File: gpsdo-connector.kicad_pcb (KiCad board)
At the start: 2 copper layers, 100 x 133.5 mm, 41 parts, among them J101 NEB21R, J102 Conn_02x05_Odd_Even, J103 Conn_02x05_Top_Bottom, J104 FPC-50-0.5MM, J105 Conn_02x03_Top_Bottom, J106 Conn_02x03_Top_Bottom, J107 Conn_02x05_Top_Bottom, J108 Conn_01x02, J109 Conn_02x05_Top_Bottom, U201 APE8865N-33-HF-3, U202 LMR14030SDDAR, U301 MAX3232

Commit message: VE7XEN BBB Carrier rev 1
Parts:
- removed C201, C210: 4.7u, Capacitor_SMD:C_0805_2012Metric
- removed C202: 270pF, Capacitor_SMD:C_0805_2012Metric
- removed C203: 100nF, Capacitor_SMD:C_0805_2012Metric
- removed C204, C205: 6.8u, Capacitor_SMD:C_1206_3216Metric
- removed C206, C207: 39u, Capacitor_SMD:CP_Elec_5x5.9
- removed C208: 200n, Capacitor_SMD:C_0805_2012Metric
- removed C209: 10nF, Capacitor_SMD:C_0805_2012Metric
- removed C211: 47u, Capacitor_SMD:CP_Elec_5x5.9
- removed C301, C302, C303, C304, C305: 100n, Capacitor_SMD:C_0805_2012Metric
- removed D201: B330BE-13, Diode_SMD:D_SMB
- removed D202: ES2BA-13-F, Diode_SMD:D_SMA
- removed H101: MountingHole, MountingHole:MountingHole_3.2mm_M3_DIN965
- removed J101: NEB21R, project:NEB21R
- removed J102: Conn_02x05_Odd_Even, Connector_IDC:IDC-Header_2x05_P2.54mm_Vertical
- removed J103, J107: Conn_02x05_Top_Bottom, Connector_IDC:IDC-Header_2x05_P2.54mm_Vertical
- removed J105, J106: Conn_02x03_Top_Bottom, Connector_PinHeader_2.54mm:PinHeader_2x03_P2.54mm_Vertical
- removed J108: Conn_01x02, Connector_PinHeader_2.54mm:PinHeader_1x02_P2.54mm_Vertical
- removed J109: Conn_02x05_Top_Bottom, Connector_PinHeader_2.54mm:PinHeader_2x05_P2.54mm_Vertical
- removed L201: 2.2µH, Inductor_SMD:L_Coilcraft_XAL5030
- removed L202: 1u, Inductor_SMD:L_1206_3216Metric
- removed NT201: Net-Tie_2, NetTie:NetTie-2_SMD_Pad2.0mm
- removed R201: 25k5, Resistor_SMD:R_0805_2012Metric
- removed R202: 14k, Resistor_SMD:R_0805_2012Metric_Pad1.15x1.40mm_HandSolder
- removed R203: 10k, Resistor_SMD:R_0805_2012Metric_Pad1.15x1.40mm_HandSolder
- removed RV201: 50k, project:Trimpot_Bourns_3313J-1
- removed U201: APE8865N-33-HF-3, Package_TO_SOT_SMD:SOT-23
- removed U202: LMR14030SDDAR, Package_SO:TI_SO-PowerPAD-8
- removed U301: MAX3232, Package_SO:SOIC-16_3.9x9.9mm_P1.27mm
- added BT1: CR2032, project:CR2032-BS-6-1, B.Cu at (83.3, 92.2)
- added C1: 100nF, Capacitor_SMD:C_0805_2012Metric_Pad1.18x1.45mm_HandSolder, F.Cu at (56.6, 156.5)
- added C10: 47uF, Capacitor_SMD:C_1206_3216Metric_Pad1.33x1.80mm_HandSolder, F.Cu at (71.3, 127.8)
- added C11: 47uF, Capacitor_SMD:C_1206_3216Metric_Pad1.33x1.80mm_HandSolder, F.Cu at (71.3, 125.2)
- added C12: 100nF, Capacitor_SMD:C_0805_2012Metric_Pad1.18x1.45mm_HandSolder, F.Cu at (71.3, 122.8)
- added C13: 100n, Capacitor_SMD:C_0805_2012Metric_Pad1.18x1.45mm_HandSolder, F.Cu at (80.3, 93.2)
- added C14: 100n, Capacitor_SMD:C_0805_2012Metric_Pad1.18x1.45mm_HandSolder, F.Cu at (80.3, 82.5)
- added C15: 100n, Capacitor_SMD:C_0805_2012Metric_Pad1.18x1.45mm_HandSolder, F.Cu at (84.3, 93.2)
- added C16: 100n, Capacitor_SMD:C_0805_2012Metric_Pad1.18x1.45mm_HandSolder, F.Cu at (77.6, 89.5)
- added C17: 100n, Capacitor_SMD:C_0805_2012Metric_Pad1.18x1.45mm_HandSolder, F.Cu at (88.3, 93.2)
- added C18: 10n, Capacitor_SMD:C_0805_2012Metric_Pad1.18x1.45mm_HandSolder, F.Cu at (99.3, 139.0)
- added C19: 1uF, Capacitor_SMD:C_1206_3216Metric_Pad1.33x1.80mm_HandSolder, F.Cu at (90.8, 129.2)
- added C2: 100nF, Capacitor_SMD:C_0805_2012Metric_Pad1.18x1.45mm_HandSolder, F.Cu at (90.3, 79.0)
- added C20: 47p, Capacitor_SMD:C_0805_2012Metric_Pad1.18x1.45mm_HandSolder, F.Cu at (95.1, 140.5)
- added C21: 10pF, Capacitor_SMD:C_0805_2012Metric_Pad1.18x1.45mm_HandSolder, F.Cu at (97.8, 103.0)
- added C22: 100nF, Capacitor_SMD:C_0805_2012Metric_Pad1.18x1.45mm_HandSolder, F.Cu at (97.3, 109.2)
- added C23: 100nF, Capacitor_SMD:C_0805_2012Metric_Pad1.18x1.45mm_HandSolder, F.Cu at (92.6, 121.8)
- added C24: 100nF, Capacitor_SMD:C_0805_2012Metric_Pad1.18x1.45mm_HandSolder, F.Cu at (96.1, 115.5)
- added C3: 10uF, Capacitor_SMD:C_1206_3216Metric_Pad1.33x1.80mm_HandSolder, F.Cu at (62.0, 133.4)
- added C4: 10uF, Capacitor_SMD:C_1206_3216Metric_Pad1.33x1.80mm_HandSolder, F.Cu at (59.5, 133.4)
- added C5: 10uF, Capacitor_SMD:C_1206_3216Metric_Pad1.33x1.80mm_HandSolder, F.Cu at (62.0, 138.7)
- added C6: 10uF, Capacitor_SMD:C_1206_3216Metric_Pad1.33x1.80mm_HandSolder, F.Cu at (59.5, 138.7)
- added C7: 10nF, Capacitor_SMD:C_0805_2012Metric_Pad1.18x1.45mm_HandSolder, F.Cu at (74.3, 136.0)
- added C8: 100nF, Capacitor_SMD:C_0805_2012Metric_Pad1.18x1.45mm_HandSolder, F.Cu at (64.6, 130.8)
- added C9: 330pF, Capacitor_SMD:C_0805_2012Metric_Pad1.18x1.45mm_HandSolder, F.Cu at (79.8, 134.8)
- added D1: LED, LED_SMD:LED_0805_2012Metric_Pad1.15x1.40mm_HandSolder, F.Cu at (53.1, 78.5)
- added D2: LED, LED_SMD:LED_0805_2012Metric_Pad1.15x1.40mm_HandSolder, F.Cu at (53.1, 73.2)
- added D3: LED, LED_SMD:LED_0805_2012Metric_Pad1.15x1.40mm_HandSolder, F.Cu at (53.1, 83.8)
- added D4: SS54, Diode_SMD:D_SMA, F.Cu at (68.3, 54.2)
- added D5: SS54, Diode_SMD:D_SMA, F.Cu at (70.3, 131.0)
- added D6: BAV70, Package_TO_SOT_SMD:SOT-23, F.Cu at (100.6, 110.2)
- added J1: DC-005A-2.5A-2.0, project:DC-005A-2.5A-2.0, F.Cu at (64.3, 44.0)
- added J2: SQ_OUT, project:DOSIN-801-0080, F.Cu at (105.8, 154.2)
- added J3: SINE_OUT, project:DOSIN-801-0080, F.Cu at (89.8, 154.2)
- added J4: GPS_ACT, Connector_PinHeader_2.54mm:PinHeader_1x02_P2.54mm_Vertical, F.Cu at (114.6, 53.5)
- added J5: MASTER, Connector_PinHeader_2.54mm:PinHeader_1x02_P2.54mm_Vertical, F.Cu at (54.4, 53.5)
- added L1: 1u, Inductor_SMD:L_1206_3216Metric_Pad1.22x1.90mm_HandSolder, F.Cu at (68.3, 61.2)
- added L2: 4.7uH, Inductor_SMD:L_Abracon_ASPI-0630LR, F.Cu at (78.3, 128.8)
- added L3: 10u, Inductor_SMD:L_1206_3216Metric_Pad1.22x1.90mm_HandSolder, F.Cu at (98.8, 141.5)
- added L4: 10u, Inductor_SMD:L_1206_3216Metric_Pad1.22x1.90mm_HandSolder, F.Cu at (91.3, 141.5)
- added MH2: MountingHole_3.2mm_M3_DIN965, MountingHole:MountingHole_3.2mm_M3_DIN965, F.Cu at (60.3, 52.4)
- added MH3: MountingHole_3.2mm_M3_DIN965, MountingHole:MountingHole_3.2mm_M3_DIN965, F.Cu at (105.4, 118.4)
- added MH4: MountingHole_3.2mm_M3_DIN965, MountingHole:MountingHole_3.2mm_M3_DIN965, F.Cu at (63.5, 118.4)
- added NT1: Net-Tie_2, NetTie:NetTie-2_SMD_Pad2.0mm, F.Cu at (81.8, 142.0)
- added NT2: Net-Tie_2, NetTie:NetTie-2_SMD_Pad2.0mm, F.Cu at (81.8, 139.8)
- added P8: BeagleBone_Black_Header, Connector_PinHeader_2.54mm:PinHeader_2x23_P2.54mm_Vertical, B.Cu at (61.6, 57.4)
- added P9: BeagleBone_Black_Header, Connector_PinHeader_2.54mm:PinHeader_2x23_P2.54mm_Vertical, B.Cu at (109.9, 57.4)
- added R1: 220, Resistor_SMD:R_0805_2012Metric_Pad1.20x1.40mm_HandSolder, F.Cu at (55.6, 78.5)
- added R10: 47, Resistor_SMD:R_0805_2012Metric_Pad1.20x1.40mm_HandSolder, F.Cu at (99.6, 135.5)
- added R11: 47, Resistor_SMD:R_0805_2012Metric_Pad1.20x1.40mm_HandSolder, F.Cu at (102.1, 135.5)
- added R12: 5.6k, Resistor_SMD:R_0805_2012Metric_Pad1.20x1.40mm_HandSolder, F.Cu at (115.6, 76.8)
- added R13: 5.6k, Resistor_SMD:R_0805_2012Metric_Pad1.20x1.40mm_HandSolder, F.Cu at (113.3, 76.8)
- added R14: 47, Resistor_SMD:R_0805_2012Metric_Pad1.20x1.40mm_HandSolder, F.Cu at (89.6, 116.0)
- added R15: 47, Resistor_SMD:R_0805_2012Metric_Pad1.20x1.40mm_HandSolder, F.Cu at (96.8, 121.0)
- added R16: 47, Resistor_SMD:R_0805_2012Metric_Pad1.20x1.40mm_HandSolder, F.Cu at (105.8, 140.5)
- added R2: 220, Resistor_SMD:R_0805_2012Metric_Pad1.20x1.40mm_HandSolder, F.Cu at (55.6, 73.2)
- added R3: 220, Resistor_SMD:R_0805_2012Metric_Pad1.20x1.40mm_HandSolder, F.Cu at (55.6, 83.8)
- added R4: 10k, Resistor_SMD:R_0805_2012Metric_Pad1.20x1.40mm_HandSolder, F.Cu at (68.3, 72.2)
- added R5: 15k, Resistor_SMD:R_0805_2012Metric_Pad1.20x1.40mm_HandSolder, F.Cu at (66.6, 140.2)
- added R6: 12k, Resistor_SMD:R_0805_2012Metric_Pad1.20x1.40mm_HandSolder, F.Cu at (76.6, 136.0)
- added R7: 75k, Resistor_SMD:R_0805_2012Metric_Pad1.20x1.40mm_HandSolder, F.Cu at (79.8, 137.0)
- added R8: 47, Resistor_SMD:R_0805_2012Metric_Pad1.20x1.40mm_HandSolder, F.Cu at (94.6, 135.5)
- added R9: 47, Resistor_SMD:R_0805_2012Metric_Pad1.20x1.40mm_HandSolder, F.Cu at (97.1, 135.5)
- added RV1: 20k, project:Trimpot_Bourns_3313J-1, F.Cu at (84.6, 135.8)
- added U1: LM75B, Package_SO:MSOP-8_3x3mm_P0.65mm, F.Cu at (53.6, 155.2)
- added U2: LMR14030SDDAR, Package_SO:TI_SO-PowerPAD-8, F.Cu at (68.5, 136.0)
- added U3: MAX3232, Package_SO:SOIC-16_3.9x9.9mm_P1.27mm, F.Cu at (84.3, 87.8)
- added U4: 74HC04, Package_SO:SOIC-14_3.9x8.7mm_P1.27mm, F.Cu at (97.1, 129.2)
- added U5: PCF8563T, Package_SO:SOIC-8_3.9x4.9mm_P1.27mm, F.Cu at (93.3, 107.8)
- added U6: MS5351M, Package_SO:MSOP-10_3x3mm_P0.5mm, F.Cu at (92.8, 117.2)
- added Y1: 32.768k, Crystal:Crystal_SMD_3215-2Pin_3.2x1.5mm, F.Cu at (94.6, 102.0)
- H2: renamed from H102; moved to B.Cu
- H3: renamed from H103; moved to B.Cu
- H4: renamed from H104; moved to B.Cu
- J6: renamed from J104; footprint Connector_FFC-FPC:Molex_54132-5033_1x50-1MP_P0.5mm_Horizontal -> Connector_FFC-FPC:Hirose_FH12-50S-0.5SH_1x50-1MP_P0.50mm_Horizontal
- moved H2 178.8 mm to (53.9, 65.4), turned to 180 degrees
- moved H4 178.8 mm to (53.9, 140.2), turned to 180 degrees
- moved J6 106.5 mm to (89.3, 69.1), turned to 180 degrees
- moved H3 91.0 mm to (110.5, 140.2), turned to 180 degrees
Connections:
- J6 pad 10: GND -> unconnected-(J6-Pad10)
- J6 pad 11: GND -> unconnected-(J6-Pad10)
- J6 pad 14: /UART_TX -> /GPIO[2]
- J6 pad 15: /UART_RX -> /GPIO[3]
- J6 pad 20: Net-(J104-Pad20) -> unconnected-(J6-Pad20)
- J6 pad 22: Net-(J104-Pad22) -> unconnected-(J6-Pad22)
- J6 pad 24: Net-(J104-Pad24) -> unconnected-(J6-Pad24)
- J6 pad 26: Net-(J104-Pad26) -> unconnected-(J6-Pad26)
- J6 pad 32: Net-(J104-Pad32) -> unconnected-(J6-Pad32)
- J6 pad 33: Net-(J104-Pad33) -> unconnected-(J6-Pad33)
- J6 pad 35: Net-(J104-Pad35) -> unconnected-(J6-Pad35)
- J6 pad 36: Net-(J104-Pad36) -> unconnected-(J6-Pad36)
- J6 pad 37: /OUTP_ACT -> /GPIO[60]
- J6 pad 38: Net-(J104-Pad38) -> unconnected-(J6-Pad38)
- J6 pad 39: /MACT -> /GPIO[40]
- J6 pad 41: /RESET -> /GPIO[51]
- J6 pad 45: Net-(J104-Pad45) -> unconnected-(J6-Pad45)
- J6 pad 47: Net-(J104-Pad47) -> unconnected-(J6-Pad47)
- J6 pad 49: /UART_TX_HS -> /GPIO[30]
- J6 pad 8: Net-(J104-Pad8) -> unconnected-(J6-Pad8)
- J6 pad 9: GND -> unconnected-(J6-Pad10)
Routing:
- net +3V3: track 15.4 -> 277.2 mm, vias 0 -> 8
- net /I2C2.SDA: track 0.00 -> 132.8 mm, vias 0 -> 2
- net /I2C2.SCL: track 0.00 -> 131.9 mm
- net GNDS: track 48.3 -> 138.2 mm, vias 25 -> 37
- net Net-(C5-Pad1): track 0.00 -> 85.4 mm, vias 0 -> 6
- net /GPIO[65]: track 0.00 -> 56.4 mm, vias 0 -> 2
- net Net-(J6-Pad43): track 0.00 -> 40.9 mm, vias 0 -> 2
- net /GPIO[30]: track 0.00 -> 37.2 mm, vias 0 -> 1
- net /Clock Generation/CLKIN: track 0.00 -> 36.3 mm
- net Net-(J106-Pad6): track 34.1 -> 0.00 mm, vias 2 -> 0
- net Net-(J106-Pad5): track 34.0 -> 0.00 mm, vias 2 -> 0
- net Net-(R16-Pad2): track 0.00 -> 33.4 mm
- net /Clock Generation/10M Filter/10M_IN: track 0.00 -> 31.7 mm
- net /GPIO[51]: track 0.00 -> 31.4 mm, vias 0 -> 1
- net +5V: track 103.5 -> 134.3 mm, vias 2 -> 3
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- added copper zone on F.Cu, net Net-(C5-Pad1)
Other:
- board size 100 x 133.5 mm -> 70 x 121.5 mm
- net class Default removed
- board text added: "1"
- board text added: "12-15V"
- board text added: "50"
- board text added: "Note: due to to way pin numbers work on the BBB, the connectors are actually 2.54mm pin headers with the 3D models overridden."
- board text added: "VE7XEN UCCM+BBB Carrier rev 1 2022-10-07"

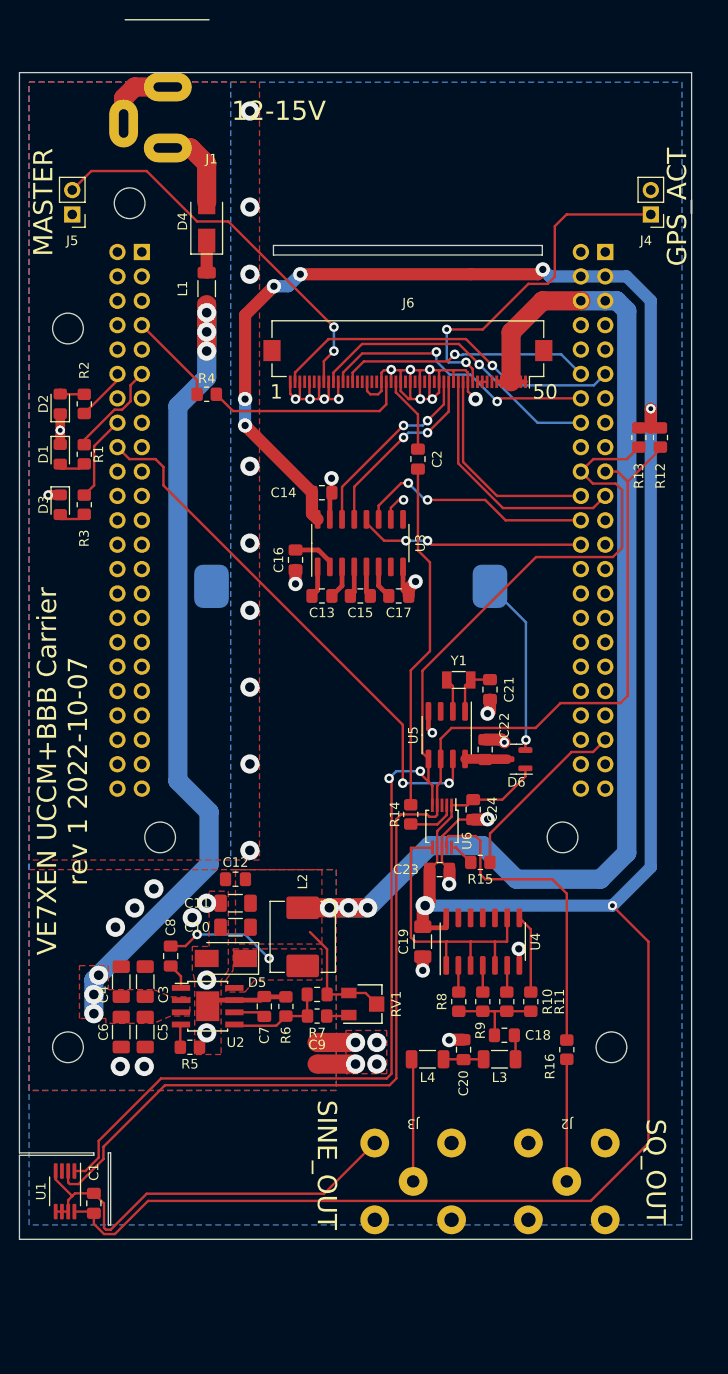
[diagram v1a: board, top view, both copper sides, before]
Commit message: rev 1 DFM fixes, kibot automation
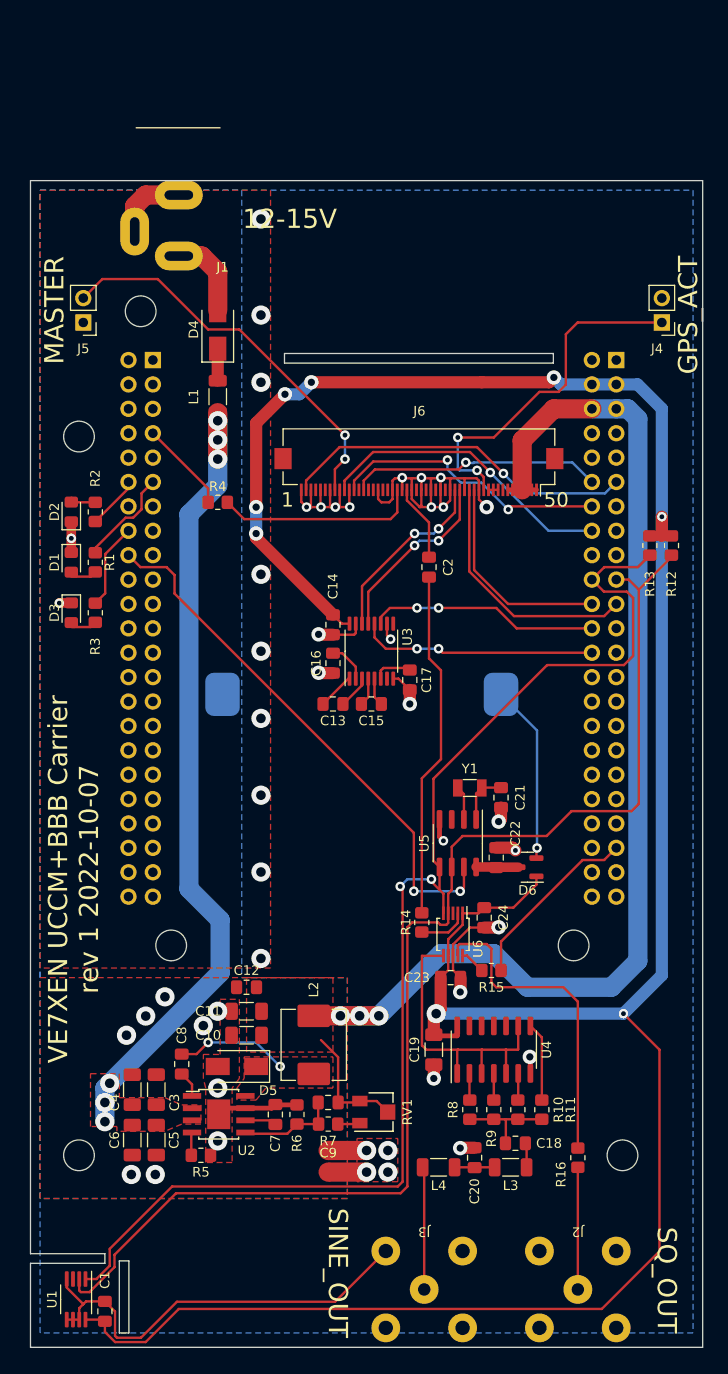
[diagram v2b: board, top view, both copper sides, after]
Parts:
- U3: footprint Package_SO:SOIC-16_3.9x9.9mm_P1.27mm -> Package_SO:TSSOP-16_4.4x5mm_P0.65mm
- moved C14 13.8 mm to (81.5, 96.2), turned to -90 degrees
- moved C16 11.4 mm to (81.5, 100.2)
- moved MH3 11.3 mm to (106.6, 129.6)
- moved MH4 11.3 mm to (64.7, 129.6)
- moved J4 11.3 mm to (115.8, 64.8)
- moved J5 11.3 mm to (55.5, 64.8)
- moved BT1 11.3 mm to (84.5, 103.5)
- moved C1 11.3 mm to (57.8, 167.8)
- moved C10 11.3 mm to (72.5, 139.0)
- moved C11 11.3 mm to (72.5, 136.5)
- moved C12 11.3 mm to (72.5, 134.0)
- moved C13 11.3 mm to (81.5, 104.5)
- moved C15 11.3 mm to (85.5, 104.5)
- moved C18 11.3 mm to (100.5, 150.2)
- moved C19 11.3 mm to (92.0, 140.5)
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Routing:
- net GNDS: track 138.2 -> 136.4 mm
- net /GPIO[15]: track 25.1 -> 24.0 mm
- net /GPIO[14]: track 23.6 -> 24.7 mm
- net +3V3: track 277.2 -> 278.2 mm
- net /RS232_RX: track 19.9 -> 19.1 mm
- net Net-(C17-Pad1): track 3.46 -> 4.06 mm
- net Net-(C13-Pad1): track 3.27 -> 3.85 mm
- net /RS232_TX: track 19.6 -> 19.1 mm
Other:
- outline, holes or cut-outs redrawn
- rule pad_to_mask_clearance: 0.051 -> 0
- board text removed: "Note: due to to way pin numbers work on the BBB, the connectors are actually 2.54mm pin headers with the 3D models overridden."

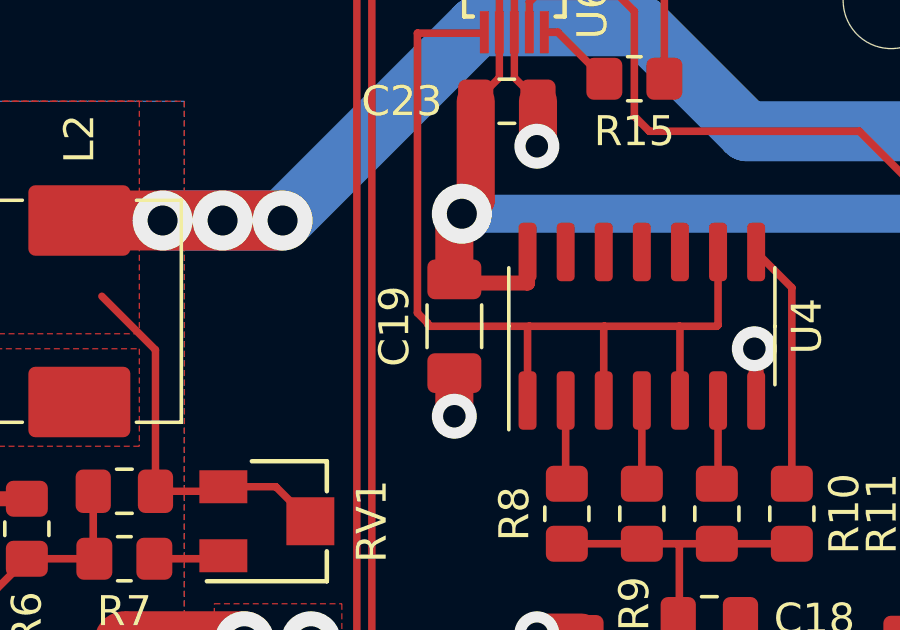
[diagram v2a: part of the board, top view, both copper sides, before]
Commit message: Fix footprint of C19 JLCPCB DFM identified 0805 part fitted on 1206 footprint
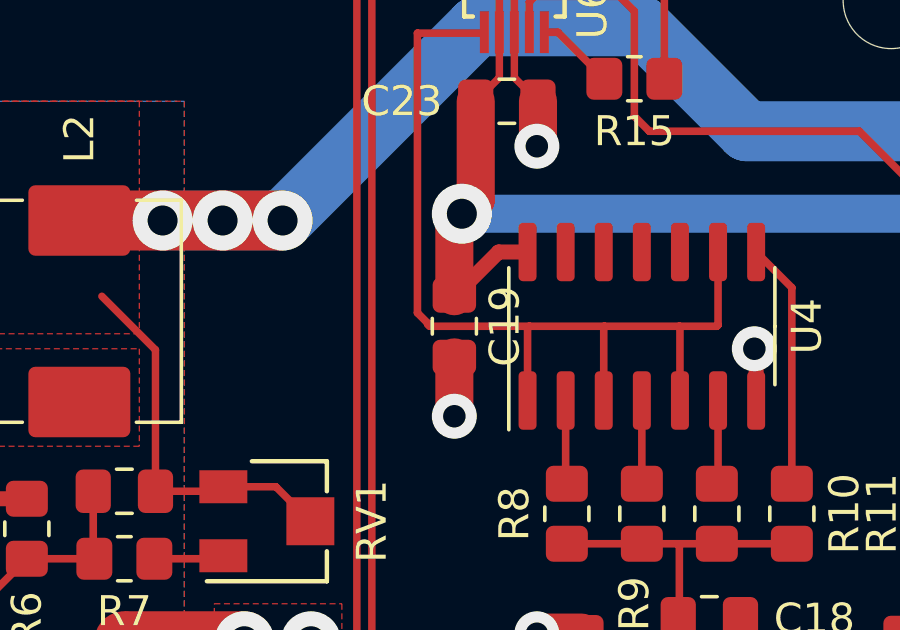
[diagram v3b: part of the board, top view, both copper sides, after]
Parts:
- C19: footprint Capacitor_SMD:C_1206_3216Metric_Pad1.33x1.80mm_HandSolder -> Capacitor_SMD:C_0805_2012Metric_Pad1.18x1.45mm_HandSolder
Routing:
- net GNDS: track 136.4 -> 136.9 mm

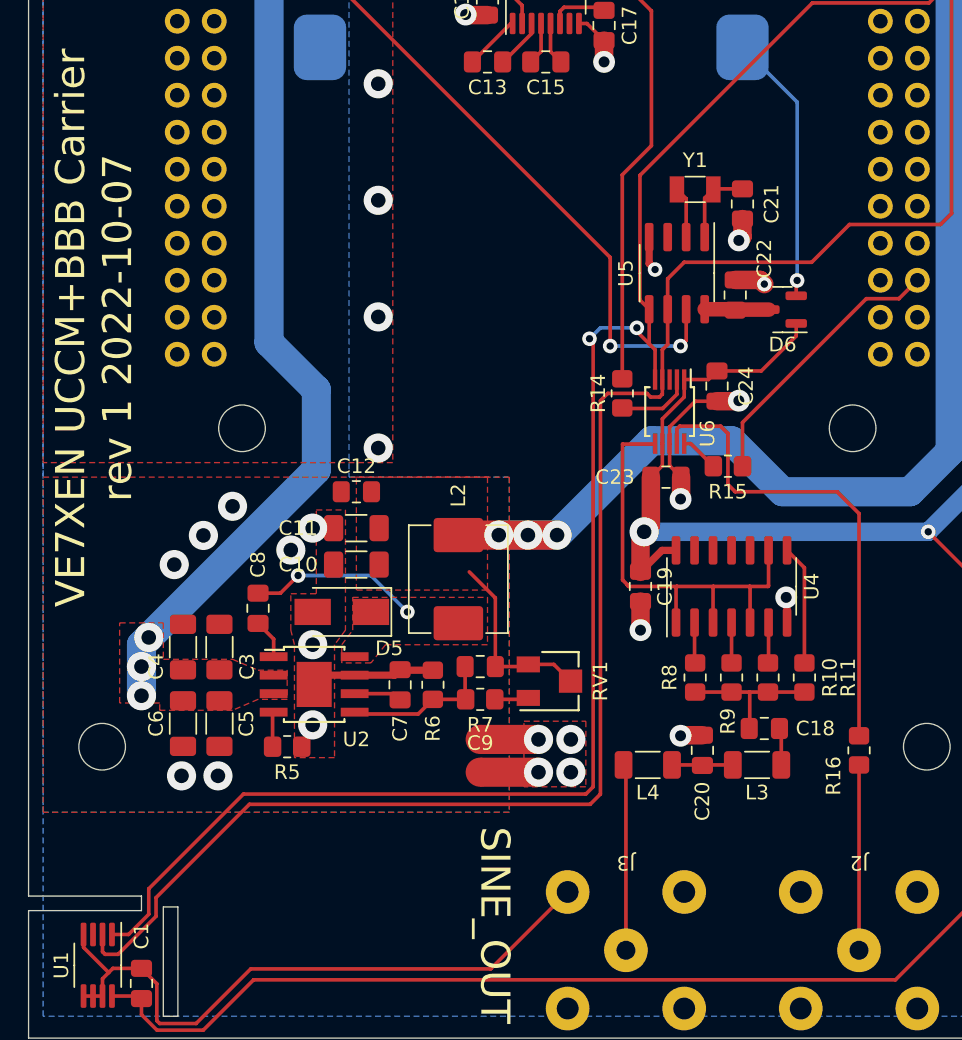
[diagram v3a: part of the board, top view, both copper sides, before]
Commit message: Fix 10M output filter
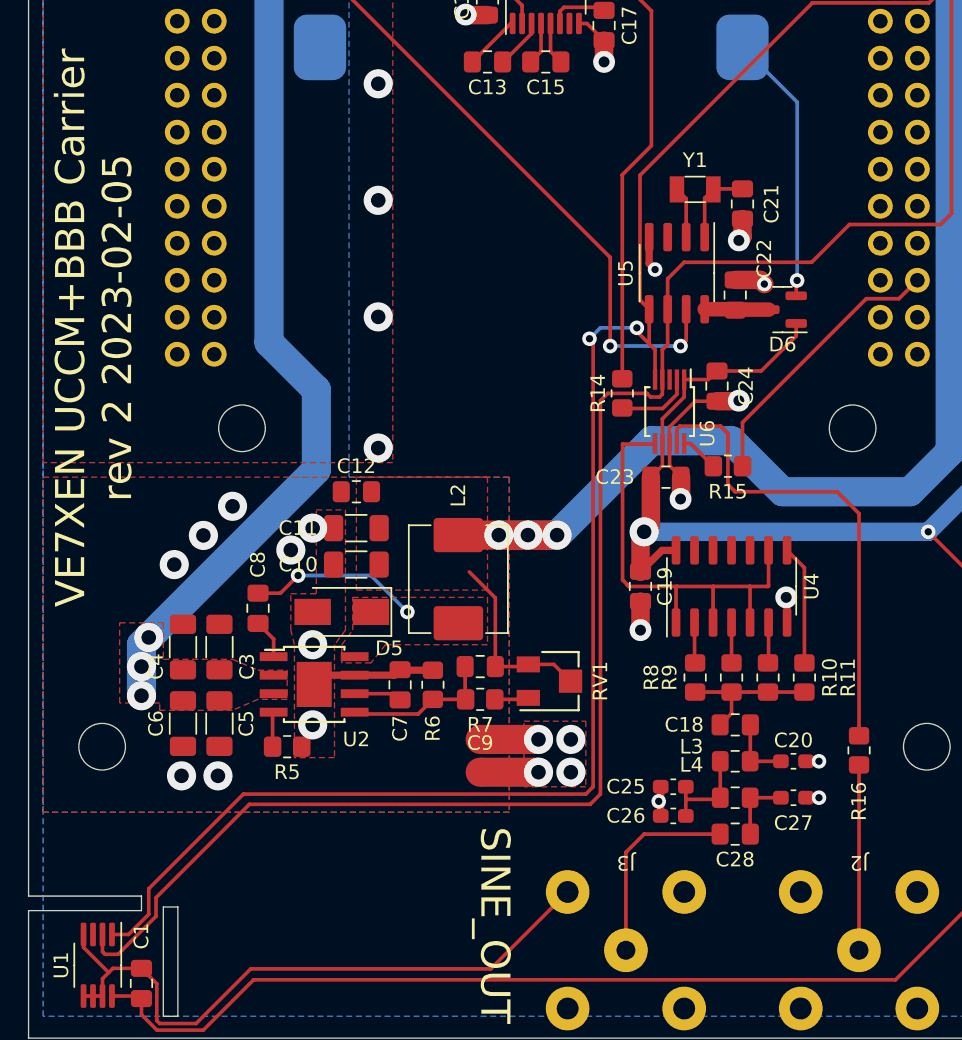
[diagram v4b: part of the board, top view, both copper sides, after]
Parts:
- added C25: 330p, Capacitor_SMD:C_0603_1608Metric_Pad1.08x0.95mm_HandSolder, F.Cu at (94.2, 154.2)
- added C26: 220p, Capacitor_SMD:C_0603_1608Metric_Pad1.08x0.95mm_HandSolder, F.Cu at (94.2, 156.2)
- added C27: 330p, Capacitor_SMD:C_0603_1608Metric_Pad1.08x0.95mm_HandSolder, F.Cu at (102.5, 155.0)
- added C28: 100nF, Capacitor_SMD:C_0805_2012Metric_Pad1.18x1.45mm_HandSolder, F.Cu at (98.5, 157.5)
- C18: value 10n -> 100nF
- C20: value 47p -> 330p; footprint Capacitor_SMD:C_0805_2012Metric_Pad1.18x1.45mm_HandSolder -> Capacitor_SMD:C_0603_1608Metric_Pad1.08x0.95mm_HandSolder
- L3, L4: value 10u -> 1u; footprint Inductor_SMD:L_1206_3216Metric_Pad1.22x1.90mm_HandSolder -> Inductor_SMD:L_0805_2012Metric_Pad1.15x1.40mm_HandSolder
- R10, R11, R8, R9: value 47 -> 200
- moved L4 6.41 mm to (98.5, 155.0), turned to 0 degrees
- moved C20 6.29 mm to (102.5, 152.5), turned to 0 degrees
- moved C18 2.02 mm to (98.5, 150.0), turned to 180 degrees
- moved L3 1.52 mm to (98.5, 152.5)
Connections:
- C18 pad 1: Net-(C18-Pad1) -> Net-(C20-Pad1)
- L3 pad 1: Net-(C18-Pad2) -> Net-(C20-Pad1)
- L3 pad 2: Net-(C20-Pad1) -> Net-(L3-Pad2)
- L4 pad 1: Net-(C20-Pad1) -> Net-(L3-Pad2)
- L4 pad 2: /Clock Generation/CLK2SINE -> Net-(C27-Pad1)
- R10 pad 2: Net-(C18-Pad1) -> Net-(C18-Pad2)
- R11 pad 2: Net-(C18-Pad1) -> Net-(C18-Pad2)
- R8 pad 2: Net-(C18-Pad1) -> Net-(C18-Pad2)
- R9 pad 2: Net-(C18-Pad1) -> Net-(C18-Pad2)
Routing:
- net Net-(C18-Pad1): track 10.0 -> 0.00 mm
- net Net-(C18-Pad2): track 2.55 -> 10.1 mm
- net Net-(L3-Pad2): track 0.00 -> 6.91 mm
- net Net-(C27-Pad1): track 0.00 -> 4.62 mm
- net GNDS: track 136.9 -> 139.3 mm, vias 37 -> 39
- net /Clock Generation/CLK2SINE: track 12.8 -> 13.7 mm
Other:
- board text added: "VE7XEN UCCM+BBB Carrier rev 2 2023-02-05"
- board text removed: "VE7XEN UCCM+BBB Carrier rev 1 2022-10-07"
